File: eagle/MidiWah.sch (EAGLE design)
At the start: 33 parts, among them IC1 ATMEGA168, IC2 7805L, IC3 MCP4251, IC4 6N138

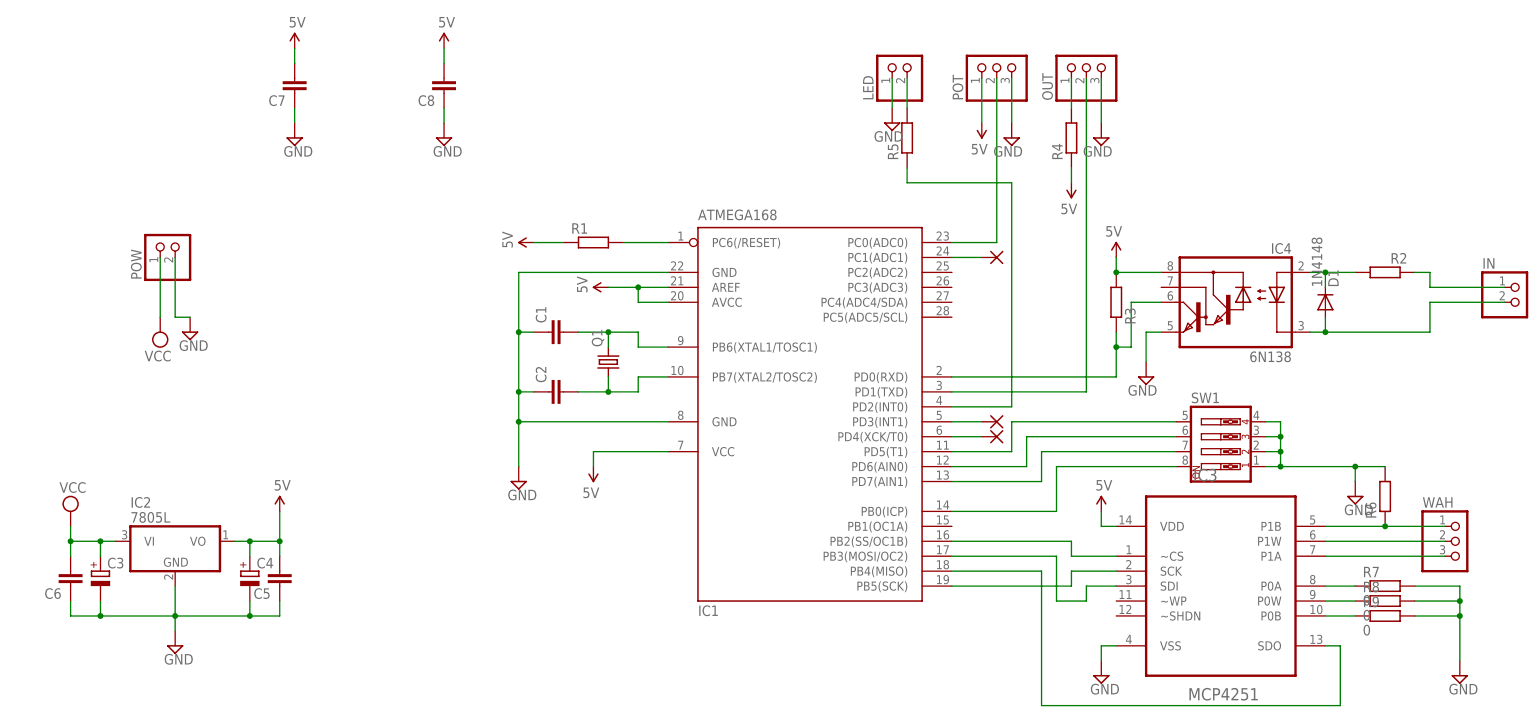
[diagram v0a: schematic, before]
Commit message: Added board render and BOM
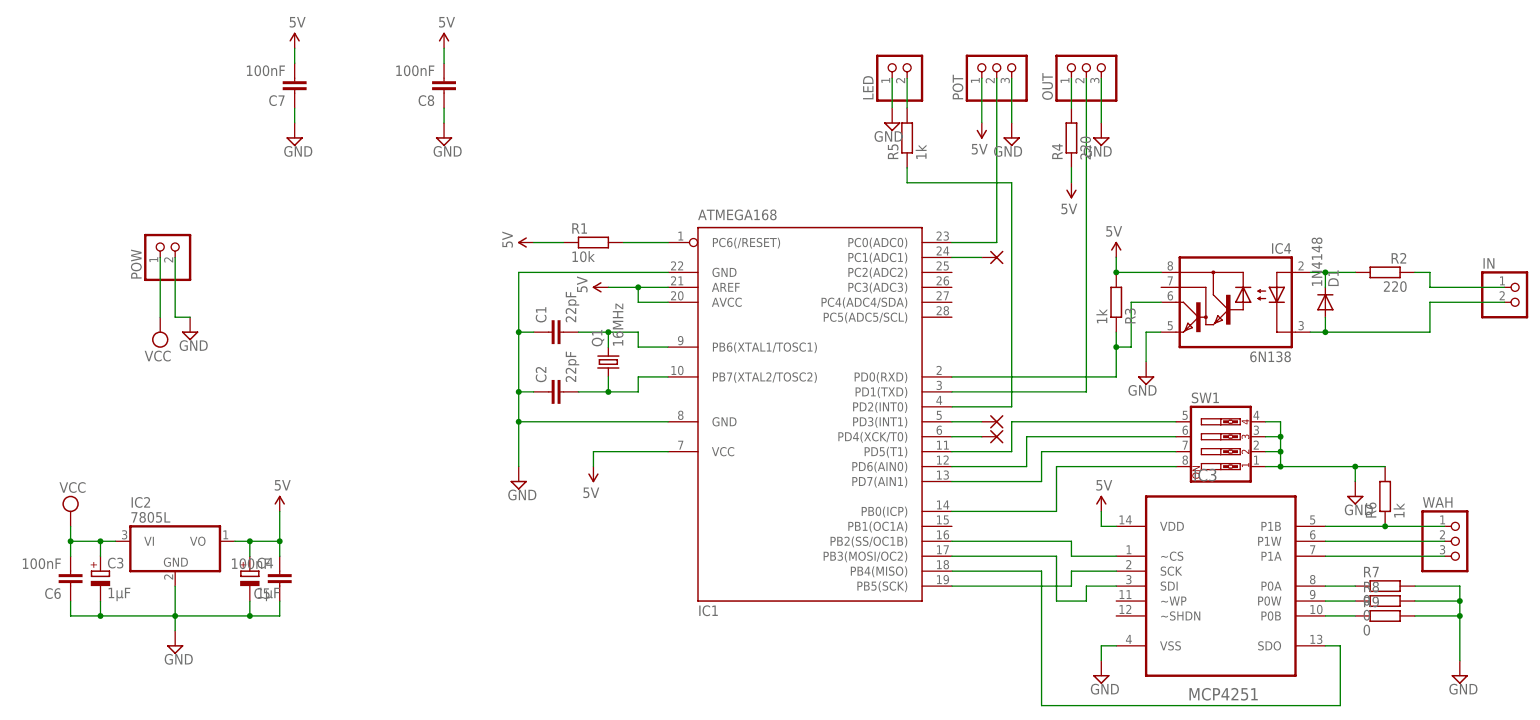
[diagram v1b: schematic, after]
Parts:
- C1, C2: value (none) -> 22pF
- C3, C4: value (none) -> 1µF
- C5, C6, C7, C8: value (none) -> 100nF
- Q1: value (none) -> 16MHz
- R1: value (none) -> 10k
- R2, R4: value (none) -> 220
- R3, R5, R6: value (none) -> 1k
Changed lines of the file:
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@@
 <?xml version="1.0" encoding="utf-8"?>
 <!DOCTYPE eagle SYSTEM "eagle.dtd">
-<eagle version="6.4">
+<eagle version="7.1.0">
 <drawing>
 <settings>
@@
 </classes>
 <parts>
-<part name="Q1" library="crystal" deviceset="CRYSTAL" device="HC49S"/>
+<part name="Q1" library="crystal" deviceset="CRYSTAL" device="HC49S" value="16MHz"/>
 <part name="IC4" library="optocoupler" deviceset="6N138" device=""/>
 <part name="SW1" library="special" deviceset="SW_DIP-4" device=""/>
 <part name="IC1" library="atmel" deviceset="MEGA8-P" device="" value="ATMEGA168"/>
 <part name="IC2" library="linear" deviceset="78*" device="L" technology="05"/>
-<part name="R1" library="rcl" deviceset="R-EU_" device="0204/7"/>
-<part name="C1" library="rcl" deviceset="C-EU" device="025-024X044"/>
-<part name="C2" library="rcl" deviceset="C-EU" device="025-024X044"/>
+<part name="R1" library="rcl" deviceset="R-EU_" device="0204/7" value="10k"/>
+<part name="C1" library="rcl" deviceset="C-EU" device="025-024X044" value="22pF"/>
+<part name="C2" library="rcl" deviceset="C-EU" device="025-024X044" value="22pF"/>
 <part name="U$2" library="SparkFun" deviceset="5V" device=""/>
 <part name="U$4" library="SparkFun" deviceset="5V" device=""/>
@@
 <part name="SUPPLY5" library="supply2" deviceset="GND" device=""/>
 <part name="SUPPLY6" library="supply2" deviceset="VCC" device=""/>
-<part name="C3" library="rcl" deviceset="CPOL-EU" device="E2.5-5"/>
-<part name="C4" library="rcl" deviceset="CPOL-EU" device="E2.5-5"/>
-<part name="C5" library="rcl" deviceset="C-EU" device="025-024X044"/>
-<part name="C6" library="rcl" deviceset="C-EU" device="025-024X044"/>
+<part name="C3" library="rcl" deviceset="CPOL-EU" device="E2.5-5" value="1µF"/>
+<part name="C4" library="rcl" deviceset="CPOL-EU" device="E2.5-5" value="1µF"/>
+<part name="C5" library="rcl" deviceset="C-EU" device="025-024X044" value="100nF"/>
+<part name="C6" library="rcl" deviceset="C-EU" device="025-024X044" value="100nF"/>
 <part name="U$7" library="SparkFun" deviceset="5V" device=""/>
 <part name="IC3" library="Microchip_By_element14_Batch_1" deviceset="MCP4251-104E/P" device="" value="MCP4251"/>
-<part name="R2" library="rcl" deviceset="R-EU_" device="0204/7"/>
+<part name="R2" library="rcl" deviceset="R-EU_" device="0204/7" value="220"/>
 <part name="D1" library="diode" deviceset="1N4148" device="DO35-7" value="1N4148"/>
-<part name="R3" library="rcl" deviceset="R-EU_" device="0204/7"/>
+<part name="R3" library="rcl" deviceset="R-EU_" device="0204/7" value="1k"/>
 <part name="SUPPLY3" library="supply2" deviceset="GND" device=""/>
 <part name="POT" library="pinhead" deviceset="PINHD-1X3" device=""/>
@@
 <part name="SUPPLY9" library="supply2" deviceset="GND" device=""/>
 <part name="OUT" library="pinhead" deviceset="PINHD-1X3" device=""/>
-<part name="R4" library="rcl" deviceset="R-EU_" device="0204/7"/>
+<part name="R4" library="rcl" deviceset="R-EU_" device="0204/7" value="220"/>
 <part name="SUPPLY10" library="supply2" deviceset="GND" device=""/>
 <part name="U$9" library="SparkFun" deviceset="5V" device=""/>
 <part name="LED" library="pinhead" deviceset="PINHD-1X2" device=""/>
 <part name="SUPPLY11" library="supply2" deviceset="GND" device=""/>
-<part name="R5" library="rcl" deviceset="R-EU_" device="0204/7"/>
-<part name="R6" library="rcl" deviceset="R-EU_" device="0204/2V"/>
-<part name="C7" library="rcl" deviceset="C-EU" device="025-024X044"/>
-<part name="C8" library="rcl" deviceset="C-EU" device="025-024X044"/>
+<part name="R5" library="rcl" deviceset="R-EU_" device="0204/7" value="1k"/>
+<part name="R6" library="rcl" deviceset="R-EU_" device="0204/2V" value="1k"/>
+<part name="C7" library="rcl" deviceset="C-EU" device="025-024X044" value="100nF"/>
+<part name="C8" library="rcl" deviceset="C-EU" device="025-024X044" value="100nF"/>
 <part name="SUPPLY13" library="supply2" deviceset="GND" device=""/>
 <part name="SUPPLY14" library="supply2" deviceset="GND" device=""/>
